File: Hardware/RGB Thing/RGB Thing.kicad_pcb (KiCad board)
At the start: 2 copper layers, 30 x 14 mm, 12 parts, among them J1 JST_SH_BM048, J2 UPDI Connection, U1 ATtiny1617

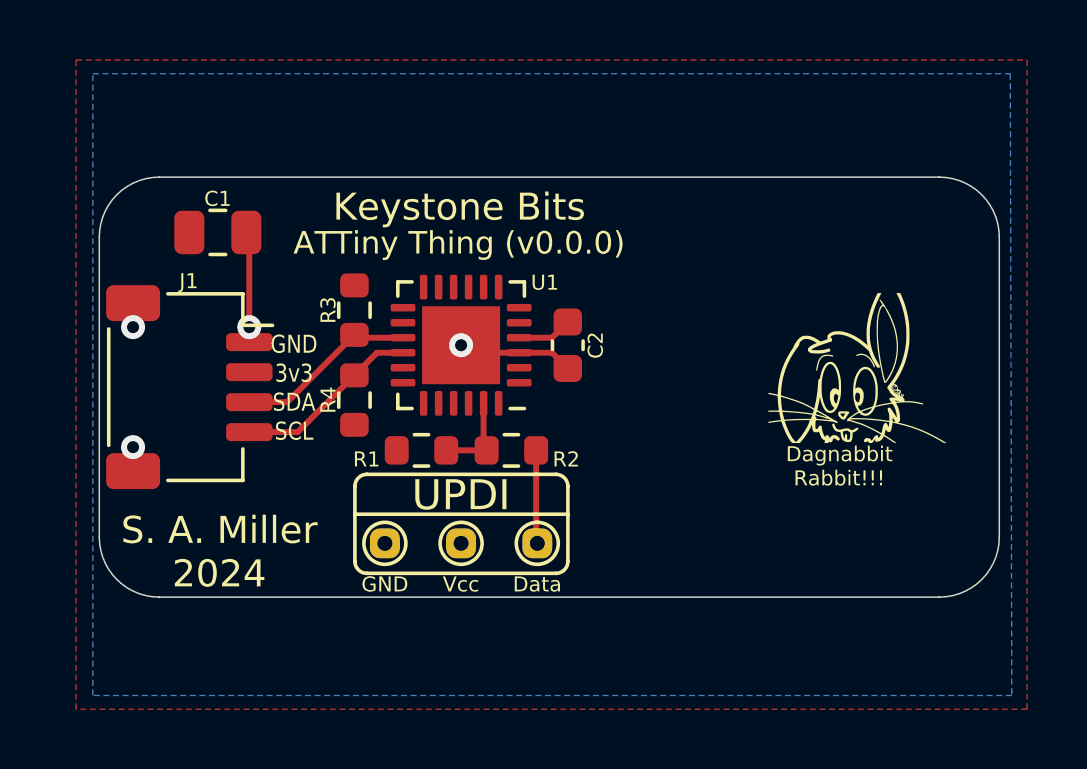
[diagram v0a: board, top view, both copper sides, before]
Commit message: Eliminated useless test points... and... NOW WITH RGB!!!
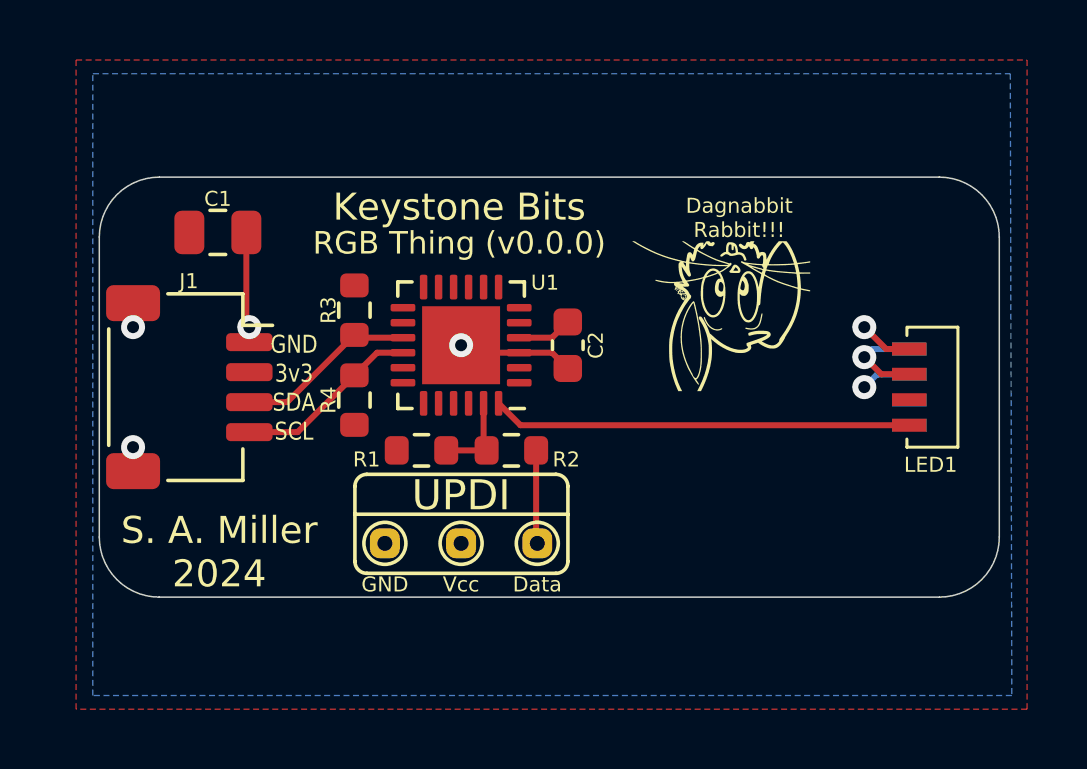
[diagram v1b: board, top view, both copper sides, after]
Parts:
- added LED1: XL-4020RGBC-WS2812B, tinker:LED-SMD_4P-L4.0-W1.7_XL-4020RGBC-WS2812B, F.Cu at (112.0, 100.0)
- added LED2: XL-4020RGBC-WS2812B, tinker:LED-SMD_4P-L4.0-W1.7_XL-4020RGBC-WS2812B, B.Cu at (112.0, 100.0)
- moved REF** 5.00 mm to (106.0, 97.0), turned to 180 degrees
- moved REF** 5.00 mm to (106.0, 103.0)
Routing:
- net PA1: track 0.00 -> 14.0 mm
- net Net-(LED1-Pad2): track 0.00 -> 3.35 mm, vias 0 -> 1
- net GND: track 7.07 -> 8.88 mm, vias 4 -> 5
- net I2C-Vcc: track 1.84 -> 3.51 mm, vias 0 -> 1
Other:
- board text removed: "The big question is... What could this little board turn into???"

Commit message: ...
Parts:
- moved C1 1.00 mm to (88.0, 95.1)
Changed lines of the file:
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@@
   )
   (footprint "Capacitor_SMD:C_0805_2012Metric" (layer "F.Cu")
-    (at 88.9508 94.8436)
+    (at 87.9856 95.0976)
     (descr "Capacitor SMD 0805 (2012 Metric), square (rectangular) end terminal, IPC_7351 nominal, (Body size source: IPC-SM-782 page 76, https://www.pcb-3d.com/wordpress/wp-content/uploads/ipc-sm-782a_amendment_1_and_2.pdf, https://docs.google.com/spreadsheets/d/1BsfQQcO9C6DZCsRaXUlFlo91Tg2WpOkGARC1WS5S8t0/edit?usp=sharing), generated with kicad-footprint-generator")
     (tags "capacitor")
@@
   (gr_arc (start 113 93) (mid 114.414214 93.585786) (end 115 95) (layer "Edge.Cuts") (width 0.05))
   (gr_line (start 85 95) (end 85 105) (layer "Edge.Cuts") (width 0.05))
-  (gr_text "${COMMENT1} (v${REVISION})" (at 97 95.2) (layer "F.SilkS")
+  (gr_text "${COMMENT1} (v${REVISION})" (at 97 95.3) (layer "F.SilkS")
     (effects (font (size 0.75 0.75) (thickness 0.15)))
   )
@@
     (effects (font (size 0.6 0.5) (thickness 0.05)))
   )
-  (segment (start 89.9008 97.9008) (end 90 98) (width 0.2) (layer "F.Cu") (net 1))
   (segment (start 111.23 98.73) (end 110.5 98) (width 0.2) (layer "F.Cu") (net 1))
+  (segment (start 88.9356 96.9356) (end 90 98) (width 0.2) (layer "F.Cu") (net 1))
   (segment (start 98.9975 98.8528) (end 97.31 98.8528) (width 0.2) (layer "F.Cu") (net 1))
-  (segment (start 89.9008 94.8436) (end 89.9008 97.9008) (width 0.2) (layer "F.Cu") (net 1))
   (segment (start 98.9975 98.8528) (end 100.091 98.8528) (width 0.2) (layer "F.Cu") (net 1))
   (segment (start 97.31 98.8528) (end 97.06 98.6028) (width 0.2) (layer "F.Cu") (net 1))
   (segment (start 100.091 98.8528) (end 100.616 99.3778) (width 0.2) (layer "F.Cu") (net 1))
+  (segment (start 88.9356 95.0976) (end 88.9356 96.9356) (width 0.2) (layer "F.Cu") (net 1))
   (segment (start 112 98.73) (end 111.23 98.73) (width 0.2) (layer "F.Cu") (net 1))
   (via (at 86.125 102) (size 0.8) (drill 0.4) (layers "F.Cu" "B.Cu") (net 1))
